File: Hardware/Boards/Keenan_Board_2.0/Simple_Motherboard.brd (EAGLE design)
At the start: 146.1 x 133.3 mm, 94 parts, among them U1 WIZ811MJ, U1_MUX 74HC4052D,653, U2_MUX 74HC4052D,653, U3_MUX 74HC4052D,653, U4_MUX 74HC4052D,653, U5_MUX 74HC4052D,653, U7_MUX 74HC4052D,653

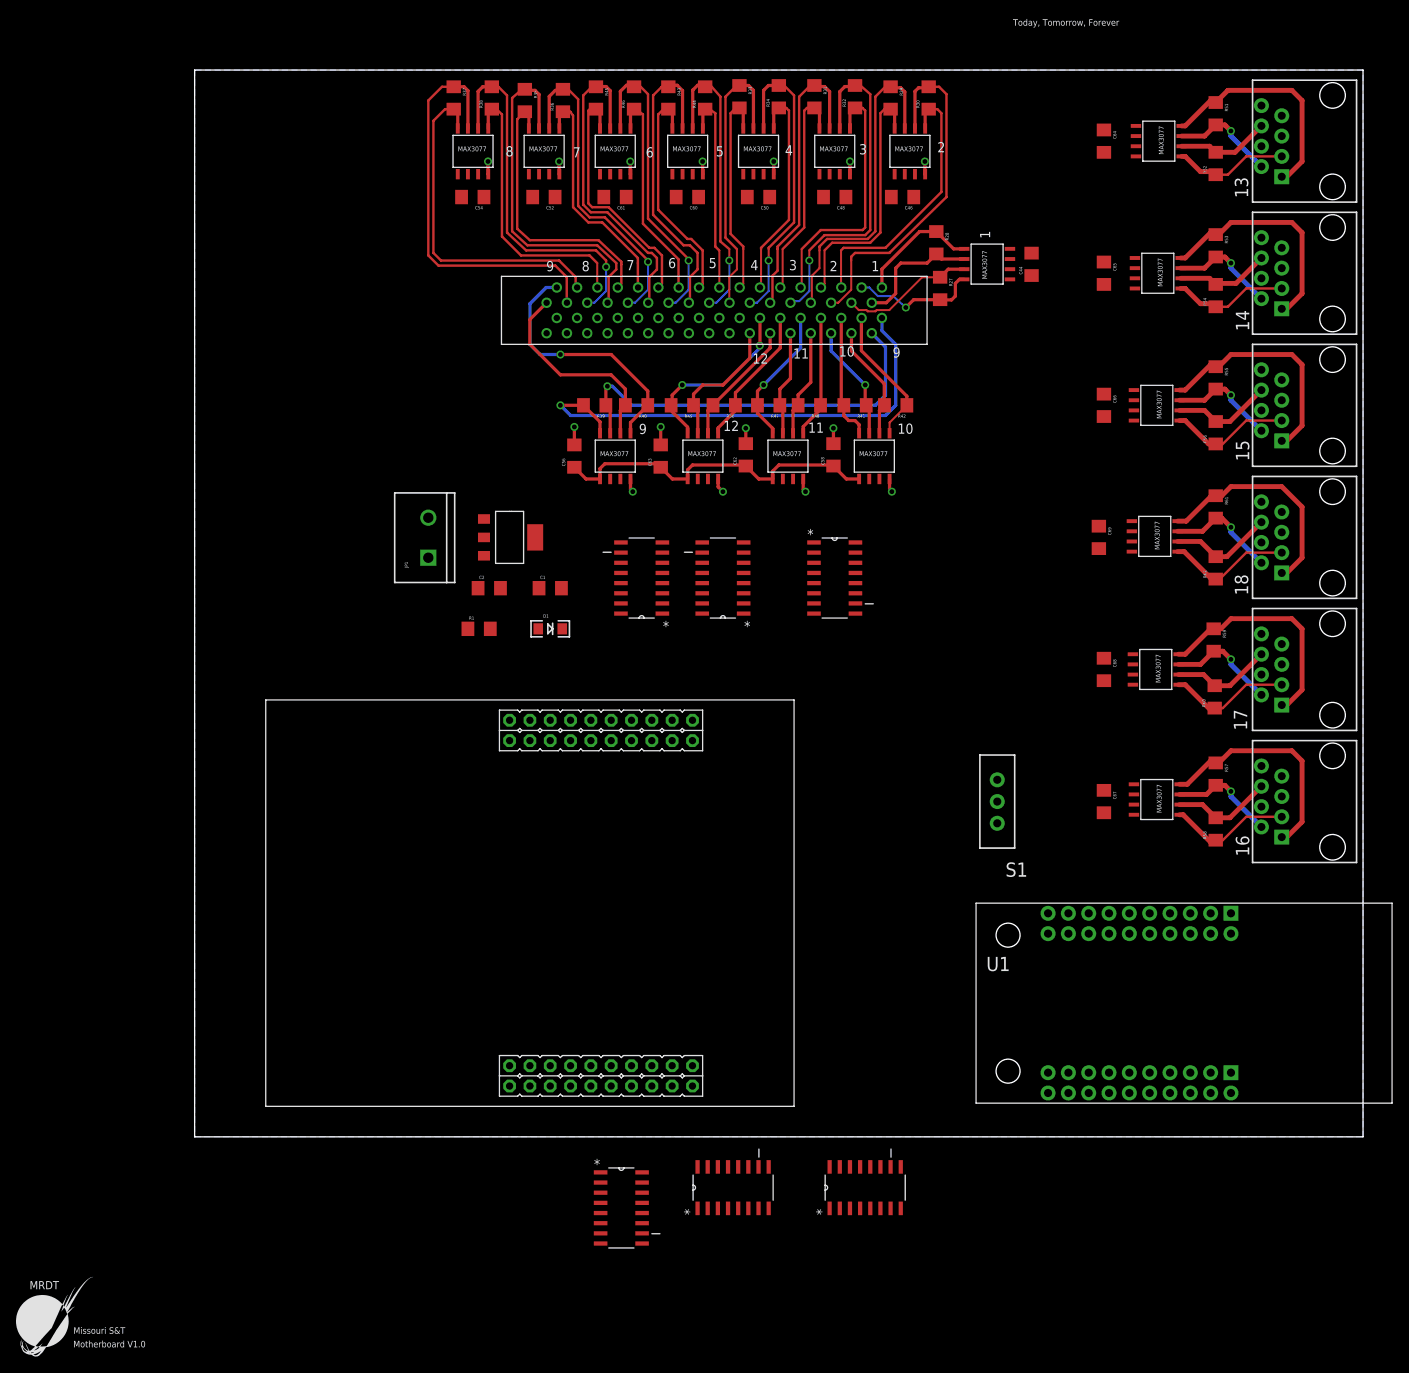
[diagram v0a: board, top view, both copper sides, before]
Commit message: Added decoupling caps for muxes
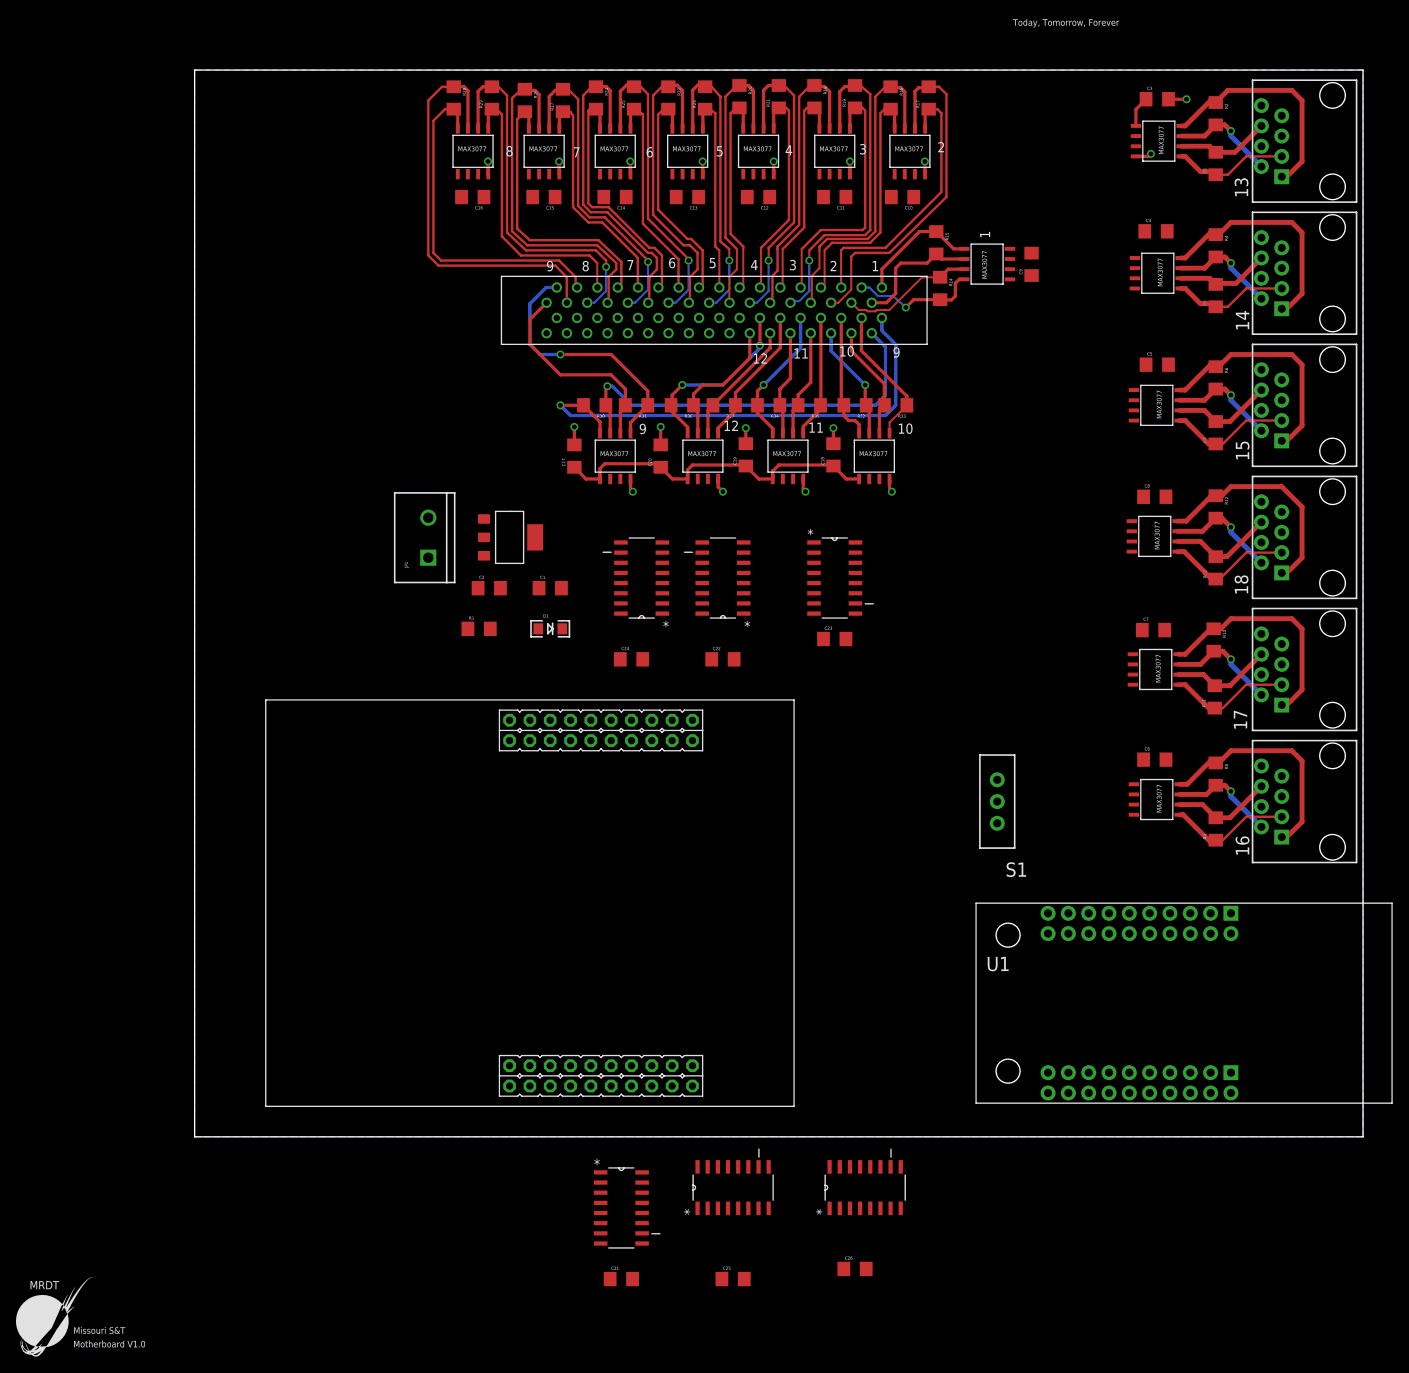
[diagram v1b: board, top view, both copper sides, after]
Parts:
- removed C64, C65, C66, C67, C68, C69: 0.1uF, SparkFun-Passives:1206
- removed R38, R39, R40, R41, R42, R47, R48, R49, R50: 120, SparkFun-Passives:1206
- added C21, C22, C23, C24, C25, C26, C3, C4, C5, C6, C7, C8: 0.1uF, SparkFun-Passives:1206
- added R14, R15, R16, R17, R18, R19, R20, R21, R26: 120, SparkFun-Passives:1206
- U$1: value RJ45-8PTH -> LD1117; device SparkFun-Connectors:RJ45-8 -> LD1117:LD1117SOT-223
- U$2: value LD1117 -> STELLARIS-LAUNCHPADSTELLARIS-LAUNCHPAD-XL; device LD1117:LD1117SOT-223 -> StellarisLaunchPad_Fred:LAUNCHPAD-XL
- U$8: value STELLARIS-LAUNCHPADSTELLARIS-LAUNCHPAD-XL -> RJ45-8PTH; device StellarisLaunchPad_Fred:LAUNCHPAD-XL -> SparkFun-Connectors:RJ45-8
- moved U$8 151.1 mm to (142.2, 74.9), turned to 90 degrees
- moved U$1 114.2 mm to (39.4, 74.9), turned to 270 degrees
- moved U$2 77.4 mm to (8.89, 3.81), turned to 0 degrees
- moved RS_TRANS_8 63.0 mm to (34.8, 123.2)
- moved R28 63.0 mm to (32.4, 129.9)
- moved R30 56.7 mm to (50.0, 91.4), turned to 180 degrees
- moved R27 52.7 mm to (46.0, 129.5), turned to 90 degrees
- moved R35 52.1 mm to (76.8, 91.4), turned to 180 degrees
- moved R37 51.2 mm to (66.2, 91.4), turned to 180 degrees
- moved RS_TRANS_10 50.0 mm to (85.0, 85.1)
- moved R29 49.8 mm to (37.1, 129.9), turned to 90 degrees
- moved U$5 49.5 mm to (142.2, 91.4)
- moved R31 44.5 mm to (55.2, 91.4), turned to 180 degrees
- moved R33 43.2 mm to (87.6, 91.4), turned to 180 degrees
- moved R36 40.9 mm to (61.0, 91.4), turned to 180 degrees
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- renumbered C44 to C9, C46 to C10, C48 to C11, C50 to C12, C52 to C15, C54 to C16, C56 to C17, C58 to C18, C60 to C13, C61 to C14, C62 to C19, C63 to C20, R43 to R22, R44 to R23, R45 to R24, R46 to R25, R51 to R2, R52 to R3, R53 to R4, R54 to R5, R55 to R6, R56 to R7, R57 to R8, R58 to R9, R59 to R10, R60 to R11, R61 to R12, R62 to R13, U$36 to U$9
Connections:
- new net VCC: U2_MUX.16, U3_MUX.16, U4_MUX.16, U5_MUX.16, U7_MUX.16
- net +3V3: now also C3.1, C4.1, C5.1, C6.1, C7.1, C8.1, U$1.VOUT; no longer C64.1, C65.1, C66.1, C67.1, C68.1, C69.1, U$2.VOUT
- net +5V: now also C21.1, C22.1, C23.1, C24.1, C25.1, C26.1, U$1.VIN; no longer U$2.VIN, U2_MUX.16, U3_MUX.16, U4_MUX.16, U5_MUX.16, U7_MUX.16
- net 10_RX+: now also R32.2, RS_TRANS_10.A; no longer R41.2, RS_TRANS_8.A
- net 10_RX-: now also R32.1, RS_TRANS_10.B; no longer R41.1, RS_TRANS_8.B
- net 10_TX+: now also R33.1, RS_TRANS_10.Y; no longer R42.1, RS_TRANS_8.Y
- net 10_TX-: now also R33.2, RS_TRANS_10.Z; no longer R42.2, RS_TRANS_8.Z
- net 11_RX+: now also R34.2; no longer R47.2
- net 11_RX-: now also R34.1; no longer R47.1
- net 11_TX+: now also R35.1; no longer R48.1
- net 11_TX-: now also R35.2; no longer R48.2
- net 12_RX+: now also R36.2; no longer R49.2
- net 12_RX-: now also R36.1; no longer R49.1
- net 12_TX+: now also R37.1; no longer R50.1
- net 12_TX-: now also R37.2; no longer R50.2
- net 1_RX+: now also R14.2; no longer R27.2
- net 1_RX-: now also R14.1; no longer R27.1
- net 1_TX+: now also R15.1; no longer R28.1
- net 1_TX-: now also R15.2; no longer R28.2
- net 2_RX+: now also R16.2; no longer R29.2
- net 2_RX-: now also R16.1; no longer R29.1
- net 2_TX+: now also R17.1; no longer R30.1
- net 2_TX-: now also R17.2; no longer R30.2
- net 3.3V: now also U$2.3.3V; no longer U$8.3.3V
- net 3_RX+: now also R18.2; no longer R31.2
- net 3_RX-: now also R18.1; no longer R31.1
- net 3_TX+: now also R19.1; no longer R32.1
- net 3_TX-: now also R19.2; no longer R32.2
- net 4_RX+: now also R20.2; no longer R33.2
- net 4_RX-: now also R20.1; no longer R33.1
- net 4_TX+: now also R21.1; no longer R34.1
- net 4_TX-: now also R21.2; no longer R34.2
- net 5_RX+: now also RS_TRANS_5.A; no longer RS_TRANS_9.A
- net 5_RX-: now also RS_TRANS_5.B; no longer RS_TRANS_9.B
- net 5_TX+: now also RS_TRANS_5.Y; no longer RS_TRANS_9.Y
- net 5_TX-: now also RS_TRANS_5.Z; no longer RS_TRANS_9.Z
- net 6_RX+: now also RS_TRANS_6.A; no longer RS_TRANS_10.A
- net 6_RX-: now also RS_TRANS_6.B; no longer RS_TRANS_10.B
- net 6_TX+: now also RS_TRANS_6.Y; no longer RS_TRANS_10.Y
- net 6_TX-: now also RS_TRANS_6.Z; no longer RS_TRANS_10.Z
- net 7_RX+: now also R26.2, RS_TRANS_7.A; no longer R35.2, RS_TRANS_5.A
- net 7_RX-: now also R26.1, RS_TRANS_7.B; no longer R35.1, RS_TRANS_5.B
- net 7_TX+: now also R27.1, RS_TRANS_7.Y; no longer R36.1, RS_TRANS_5.Y
- net 7_TX-: now also R27.2, RS_TRANS_7.Z; no longer R36.2, RS_TRANS_5.Z
- net 8_RX+: now also R28.2, RS_TRANS_8.A; no longer R37.2, RS_TRANS_6.A
- net 8_RX-: now also R28.1, RS_TRANS_8.B; no longer R37.1, RS_TRANS_6.B
- net 8_TX+: now also R29.1, RS_TRANS_8.Y; no longer R38.1, RS_TRANS_6.Y
- net 8_TX-: now also R29.2, RS_TRANS_8.Z; no longer R38.2, RS_TRANS_6.Z
- net 9_RX+: now also R30.2, RS_TRANS_9.A; no longer R39.2, RS_TRANS_7.A
- net 9_RX-: now also R30.1, RS_TRANS_9.B; no longer R39.1, RS_TRANS_7.B
- net 9_TX+: now also R31.1, RS_TRANS_9.Y; no longer R40.1, RS_TRANS_7.Y
- net 9_TX-: now also R31.2, RS_TRANS_9.Z; no longer R40.2, RS_TRANS_7.Z
- net GND: now also C21.2, C22.2, C23.2, C24.2, C25.2, C26.2, C3.2, C4.2, C5.2, C6.2, C7.2, C8.2, U$1.GND, U$2.GND1, U$2.GND2; no longer C64.2, C65.2, C66.2, C67.2, C68.2, C69.2, U$2.GND, U$8.GND1, U$8.GND2
- net N$1: now also U$3.1; no longer U$1.1
- net N$10: now also U$4.1; no longer U$3.1
- net N$11: now also U$4.2; no longer U$3.2
- net N$12: now also U$4.3; no longer U$3.3
- net N$13: now also U$5.6; no longer U$4.6
- net N$14: now also U$5.1; no longer U$4.1
- net N$15: now also U$5.2; no longer U$4.2
- net N$16: now also U$5.3; no longer U$4.3
- net N$17: now also U$6.6; no longer U$5.6
- net N$18: now also U$6.1; no longer U$5.1
- net N$19: now also U$6.2; no longer U$5.2
- net N$2: now also U$3.2; no longer U$1.2
- net N$20: now also U$6.3; no longer U$5.3
- net N$21: now also U$7.6; no longer U$6.6
- net N$22: now also U$7.1; no longer U$6.1
- net N$28: now also U$7.2; no longer U$6.2
- net N$29: now also U$7.3; no longer U$6.3
- net N$3: now also U$2.VBUS; no longer U$8.VBUS
- net N$33: now also U$8.6; no longer U$7.6
- net N$34: now also U$8.1; no longer U$7.1
- net N$35: now also U$8.2; no longer U$7.2
- net N$36: now also U$8.3; no longer U$7.3
- net N$4: now also U$3.3; no longer U$1.3
- net N$8: now also U$4.6; no longer U$3.6
- net N$9: now also U$3.6; no longer U$1.6
- net RESET: now also U$2.RST; no longer U$8.RST
- net RS485_10_RX: now also RS_TRANS_10.RO; no longer RS_TRANS_8.RO
- net RS485_10_TX: now also RS_TRANS_10.DI; no longer RS_TRANS_8.DI
- net RS485_5_RX: now also RS_TRANS_5.RO; no longer RS_TRANS_9.RO
- net RS485_5_TX: now also RS_TRANS_5.DI; no longer RS_TRANS_9.DI
- net RS485_6_RX: now also RS_TRANS_6.RO; no longer RS_TRANS_10.RO
- net RS485_6_TX: now also RS_TRANS_6.DI; no longer RS_TRANS_10.DI
- net RS485_7_RX: now also RS_TRANS_7.RO; no longer RS_TRANS_5.RO
- net RS485_7_TX: now also RS_TRANS_7.DI; no longer RS_TRANS_5.DI
- net RS485_8_RX: now also RS_TRANS_8.RO; no longer RS_TRANS_6.RO
- net RS485_8_TX: now also RS_TRANS_8.DI; no longer RS_TRANS_6.DI
- net RS485_9_RX: now also RS_TRANS_9.RO; no longer RS_TRANS_7.RO
- net RS485_9_TX: now also RS_TRANS_9.DI; no longer RS_TRANS_7.DI
- net TCP_MISO: now also U$2.PA4; no longer U$8.PA4
- net TCP_MOSI: now also U$2.PA5; no longer U$8.PA5
- net TCP_SCLK: now also U$2.PA2; no longer U$8.PA2
- net TCP_SS: now also U$2.PA3; no longer U$8.PA3
- net U1RX: now also U$2.PB0; no longer U$8.PB0
- net U1TX: now also U$2.PB1; no longer U$8.PB1
- net U1_MUX_S0: now also U$2.PA6; no longer U$8.PA6
- net U1_MUX_S1: now also U$2.PA7; no longer U$8.PA7
- net U2RX: now also U$2.PD6; no longer U$8.PD6
- net U2TX: now also U$2.PD7; no longer U$8.PD7
- net U2_MUX_S0: now also U$2.PE2; no longer U$8.PE2
- net U2_MUX_S1: now also U$2.PE3; no longer U$8.PE3
- net U3RX: now also U$2.PC6; no longer U$8.PC6
- net U3TX: now also U$2.PC7; no longer U$8.PC7
- net U3_MUX_S0: now also U$2.PB2; no longer U$8.PB2
- net U3_MUX_S1: now also U$2.PB3; no longer U$8.PB3
- net U4RX: now also U$2.PC4; no longer U$8.PC4
- net U4TX: now also U$2.PC5; no longer U$8.PC5
- net U4_MUX_S0: now also U$2.PB4; no longer U$8.PB4
- net U4_MUX_S1: now also U$2.PB5; no longer U$8.PB5
- net U5RX: now also U$2.PE4; no longer U$8.PE4
- net U5TX: now also U$2.PE5; no longer U$8.PE5
- net U5_MUX_S0: now also U$2.PB6; no longer U$8.PB6
- net U5_MUX_S1: now also U$2.PB7; no longer U$8.PB7
- net U7RX: now also U$2.PE0; no longer U$8.PE0
- net U7TX: now also U$2.PE1; no longer U$8.PE1
- net U7_MUX_S0: now also U$2.PD0; no longer U$8.PD0
- net U7_MUX_S1: now also U$2.PD1; no longer U$8.PD1
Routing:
- net GND: track 26.8 -> 31.1 mm, vias 15 -> 17
- net +3V3: track 42.7 -> 46.5 mm

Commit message: Changed muxes back to 5V power.
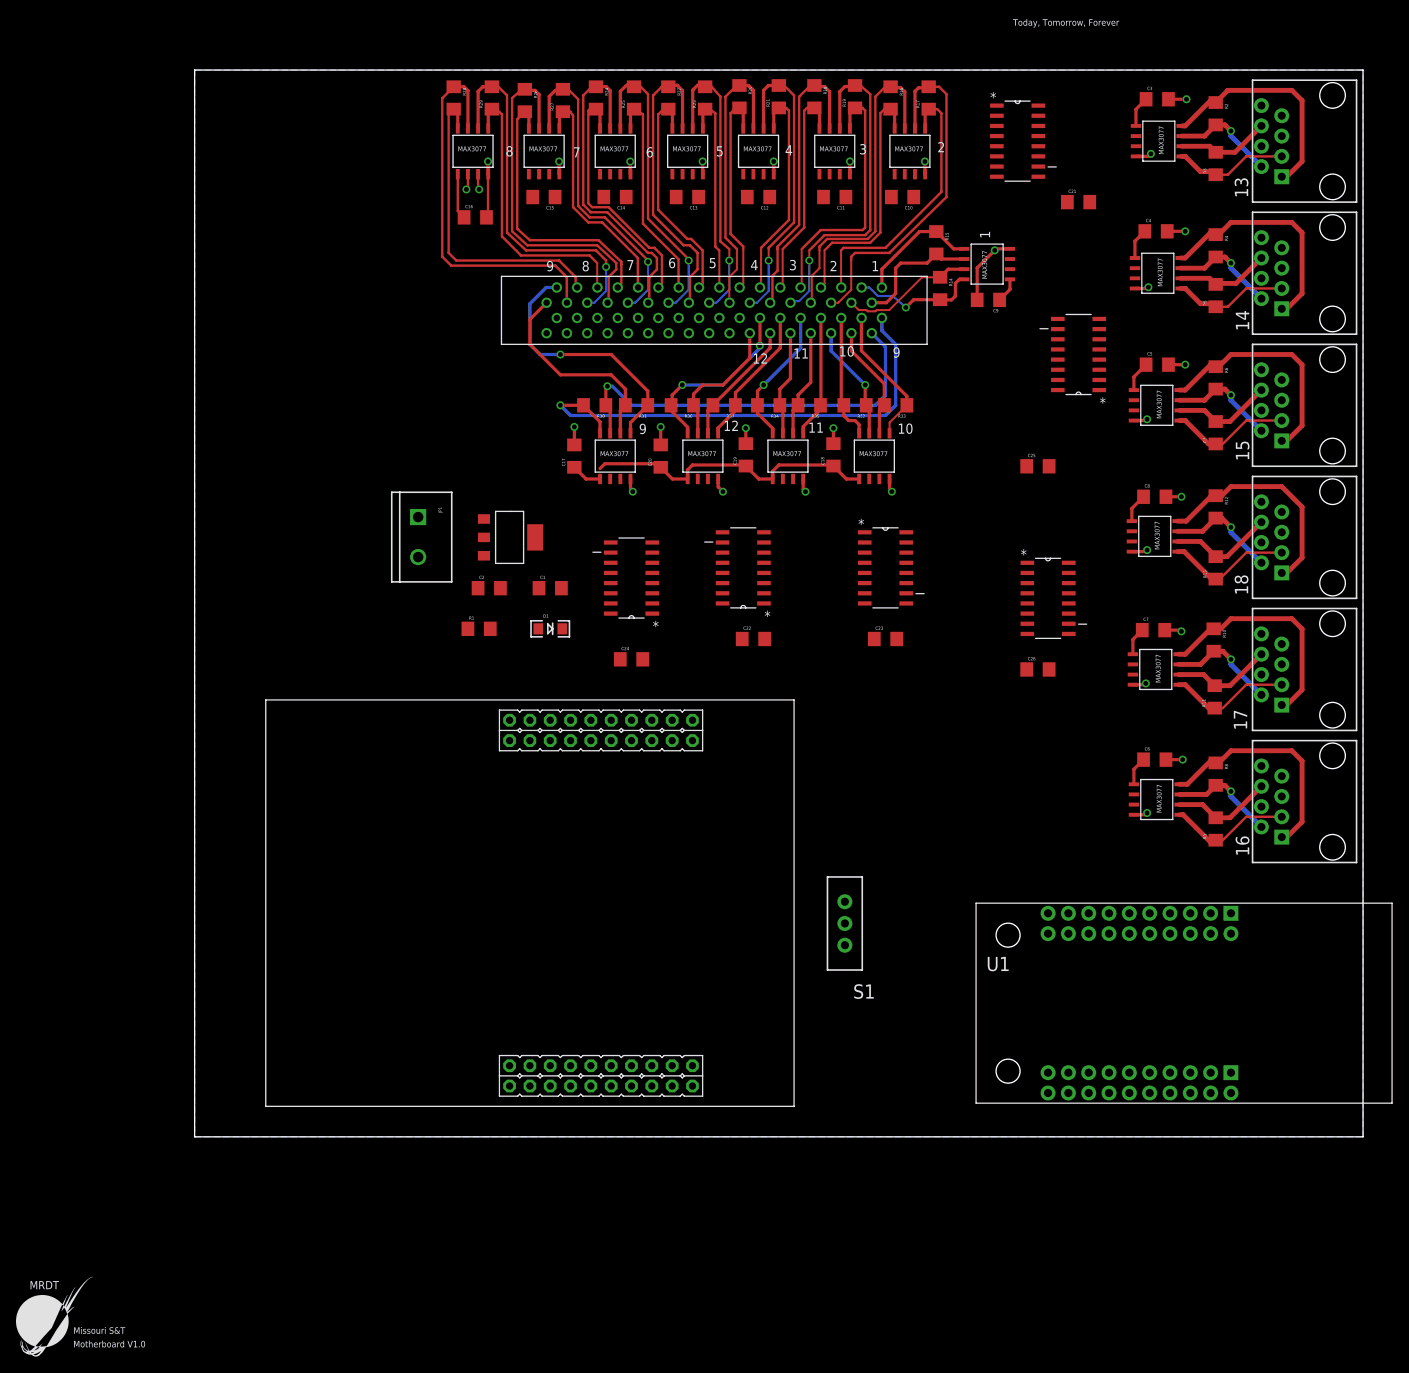
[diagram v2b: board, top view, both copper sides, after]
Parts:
- moved C21 146.2 mm to (110.5, 116.8)
- moved U1_MUX 142.3 mm to (102.9, 124.5)
- moved U5_MUX 112.7 mm to (110.5, 97.8), turned to 180 degrees
- moved C25 108.5 mm to (105.4, 83.8)
- moved C26 78.3 mm to (105.4, 58.4)
- moved U7_MUX 77.1 mm to (106.7, 67.3), turned to 0 degrees
- moved S1 24.4 mm to (81.3, 26.7)
- moved C9 6.99 mm to (99.2, 104.6), turned to 180 degrees
- moved U3_MUX 6.48 mm to (86.4, 71.1)
- moved C23 6.35 mm to (86.4, 62.2)
- moved JP1 5.24 mm to (27.9, 77.5), turned to 270 degrees
- moved C22 4.58 mm to (69.8, 62.2)
- moved U2_MUX 2.84 mm to (68.6, 71.1)
- moved C16 2.56 mm to (35.1, 114.9), turned to 0 degrees
- moved U4_MUX 1.27 mm to (54.6, 69.8)
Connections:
- net +3V3: no longer C10.1, C11.1, C12.1, C13.1, C14.1, C15.1, C16.1, C17.1, C18.1, C19.1, C20.1, C3.1, C4.1, C5.1, C6.1, C7.1, C8.1, C9.1, RS-485-1.VCC, RS-485-2.VCC, RS-485-3.VCC, RS-485-4.VCC, RS-485-5.VCC, RS-485-6.VCC, RS_TRANS_1.VCC, RS_TRANS_10.VCC, RS_TRANS_11.VCC, RS_TRANS_12.VCC, RS_TRANS_2.VCC, RS_TRANS_3.VCC, RS_TRANS_4.VCC, RS_TRANS_5.VCC, RS_TRANS_6.VCC, RS_TRANS_7.VCC, RS_TRANS_8.VCC, RS_TRANS_9.VCC
- net +5V: now also C10.1, C11.1, C12.1, C13.1, C14.1, C15.1, C16.1, C17.1, C18.1, C19.1, C20.1, C3.1, C4.1, C5.1, C6.1, C7.1, C8.1, C9.1, RS-485-1.VCC, RS-485-2.VCC, RS-485-3.VCC, RS-485-4.VCC, RS-485-5.VCC, RS-485-6.VCC, RS_TRANS_1.VCC, RS_TRANS_10.VCC, RS_TRANS_11.VCC, RS_TRANS_12.VCC, RS_TRANS_2.VCC, RS_TRANS_3.VCC, RS_TRANS_4.VCC, RS_TRANS_5.VCC, RS_TRANS_6.VCC, RS_TRANS_7.VCC, RS_TRANS_8.VCC, RS_TRANS_9.VCC
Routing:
- net +5V: track 0.00 -> 72.1 mm
- net +3V3: track 46.5 -> 0.00 mm
- net GND: track 31.1 -> 65.0 mm, vias 17 -> 28
- net 8_RX+: track 42.7 -> 39.4 mm
- net 8_RX-: track 51.6 -> 48.4 mm
- net RS485_8_RX: track 0.00 -> 1.98 mm, vias 0 -> 1
- net RS485_8_TX: track 0.00 -> 1.96 mm, vias 0 -> 1
